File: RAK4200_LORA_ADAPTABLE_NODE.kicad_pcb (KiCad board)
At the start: 2 copper layers, 75 x 49 mm, 19 parts, among them J1 Screw_Terminal_01x03, J2 Screw_Terminal_01x03, J3 Conn_01x11_Male, J4 Conn_01x11_Male, J5 Conn_01x01_Male, J6 Conn_01x11_Male, J7 Conn_01x11_Male, J8 Conn_01x11_Male, U1 RAK4200

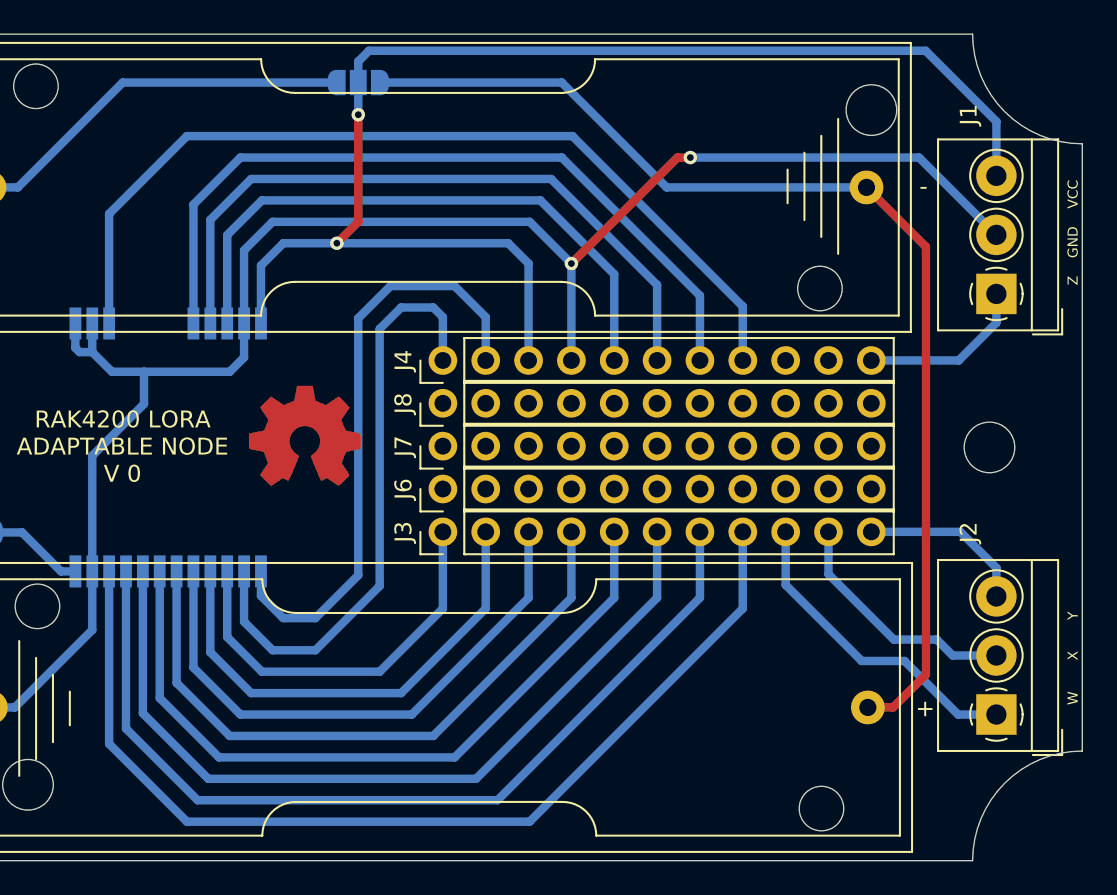
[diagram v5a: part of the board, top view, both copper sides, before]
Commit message: copper plane - single board gerbers
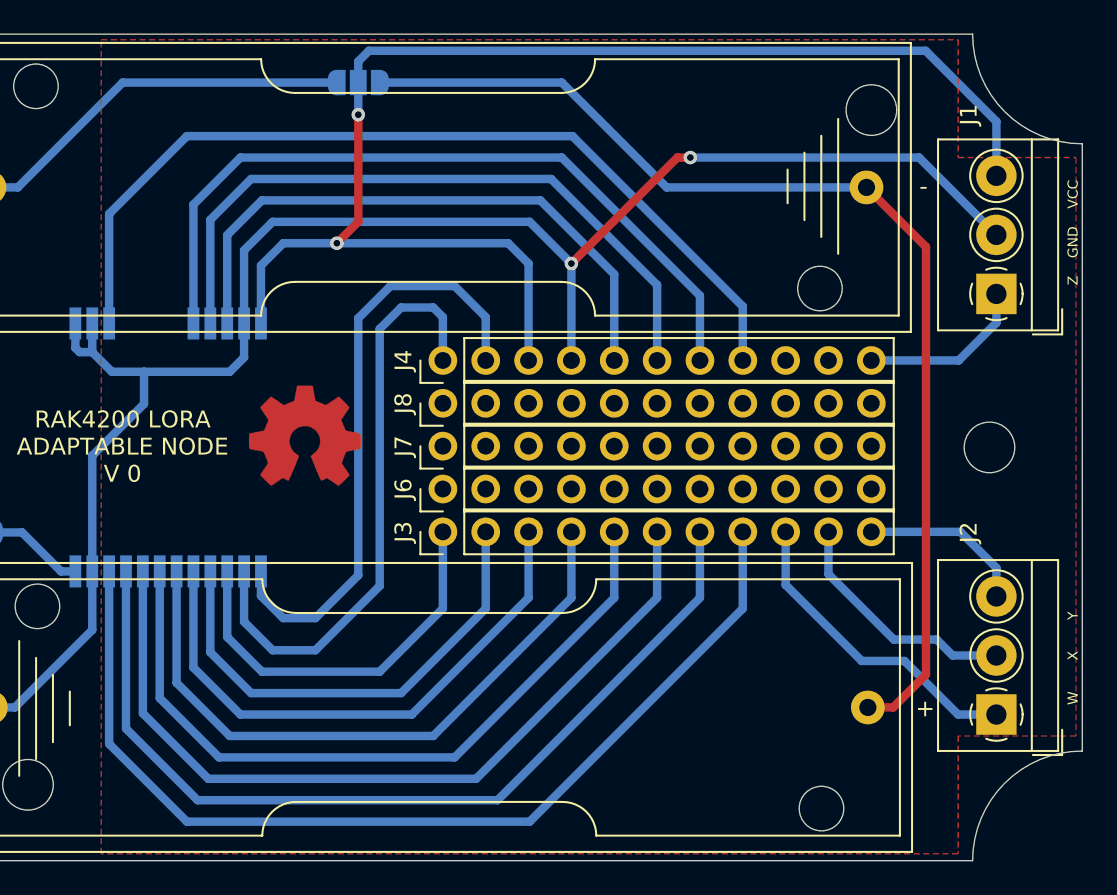
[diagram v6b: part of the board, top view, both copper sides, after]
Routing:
- added copper zone on F.Cu, net Net-(BT2-Pad2)
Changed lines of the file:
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@@
   )
   (page A4)
+  (title_block
+    (title "RAK4200 LORA ADAPTABLE NODE")
+    (company Galopago)
+  )
   (layers
     (0 F.Cu signal)
@@
     (visible_elements FFFFFF7F)
     (pcbplotparams
-      (layerselection 0x01000_ffffffff)
+      (layerselection 0x010f0_ffffffff)
       (usegerberextensions false)
       (usegerberattributes false)
@@
       (psnegative false)
       (psa4output false)
-      (plotreference false)
-      (plotvalue false)
+      (plotreference true)
+      (plotvalue true)
       (plotinvisibletext false)
       (padsonsilk true)
-      (subtractmaskfromsilk false)
-      (outputformat 5)
+      (subtractmaskfromsilk true)
+      (outputformat 1)
       (mirror false)
-      (drillshape 1)
+      (drillshape 0)
       (scaleselection 1)
       (outputdirectory "./"))
@@
   (segment (start 137.095 116.775) (end 137.095 119.345) (width 0.5) (layer B.Cu) (net 26))
   (segment (start 136.525 116.205) (end 137.095 116.775) (width 0.5) (layer B.Cu) (net 26))
+  (zone (net 3) (net_name "Net-(BT2-Pad2)") (layer F.Cu) (hatch edge 0.508)
+    (connect_pads (clearance 0.508))
+    (min_thickness 0.254)
+    (fill yes (arc_segments 32) (thermal_gap 0.508) (thermal_bridge_width 0.508))
+    (polygon
+      (pts
+        (xy 167.64 100.33) (xy 167.64 107.315) (xy 174.625 107.315) (xy 174.625 141.605) (xy 167.64 141.605)
+        (xy 167.64 148.59) (xy 116.84 148.59) (xy 116.84 100.33) (xy 139.7 100.33)
+      )
+    )
+  )
 )

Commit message: silkscreen ext ant fix
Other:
- board text added: "JP2 ANT 1-2 J5"
- board text removed: "JP2 ANT 1-2 J6"
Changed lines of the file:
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@@
     (pad 1 np_thru_hole circle (at 0 0) (size 3 3) (drill 3) (layers *.Cu *.Mask))
   )
-  (gr_text "JP2 ANT\n1-2 J6\n\n" (at 107.95 135.89) (layer B.SilkS)
+  (gr_text "JP2 ANT\n1-2 J5\n\n" (at 107.95 135.89) (layer B.SilkS)
     (effects (font (size 1 1) (thickness 0.15)) (justify mirror))
   )
